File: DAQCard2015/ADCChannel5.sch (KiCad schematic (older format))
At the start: 50 parts, among them U10 LTC6403, U6 LTC6403, U7 AD9219, U8 LTC6403, U9 LTC6403

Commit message: Replaces single ample with 4-channel varients. Greatly reducing part count
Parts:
- removed C23, C33, C37, C38: .01uF, symbol C
- removed C24, C25, C29, C31, C32: .1uF, symbol C
- removed C26, C27, C28, C34, C35, C36, C39, C40, C41, C42, C43, C44: C, symbol C
- removed C30: 2.2uF, symbol CP
- removed R25, R32, R37, R38: Rt, symbol R
- removed R26, R27, R33, R34, R39, R40, R41, R42: Ri, symbol R
- removed R29, R30, R35, R36, R43, R44, R45: Rf, symbol R
- removed R31: 10k, symbol R
- removed U10, U6, U8, U9: LTC6403, symbol LTC6403
- removed U7: AD9219, symbol AD9219
- added C62, C63, C64: C, symbol C
- added C65: .01uF, symbol C
- added C66, C67, C68, C70, C71: .1uF, symbol C
- added C69: 2.2uF, symbol CP
- added R49: Rt, symbol R
- added R50: 2.7k, symbol R
- added R51: 1k, symbol R
- added R52: 10k, symbol R
- added RP19: R_PACK8, symbol R_PACK8
- added RP20, RP21: Rf, symbol R_PACK4
- added U14: THS4524IDBTR, symbol THS4524IDBTR
- added U15: AD9219, symbol AD9219
- R46: value Rf -> Rt
- R47: value 2.7k -> Rt
- R48: value 1k -> Rt
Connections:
- net labels added: 3V3ana, VOCM
- net labels removed: 18ana, 3V3, Vocm
- wire segments 178 -> 192
- no-connect marks 12 -> 4
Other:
- note removed: "100R Termination \nis common for all ADCs."

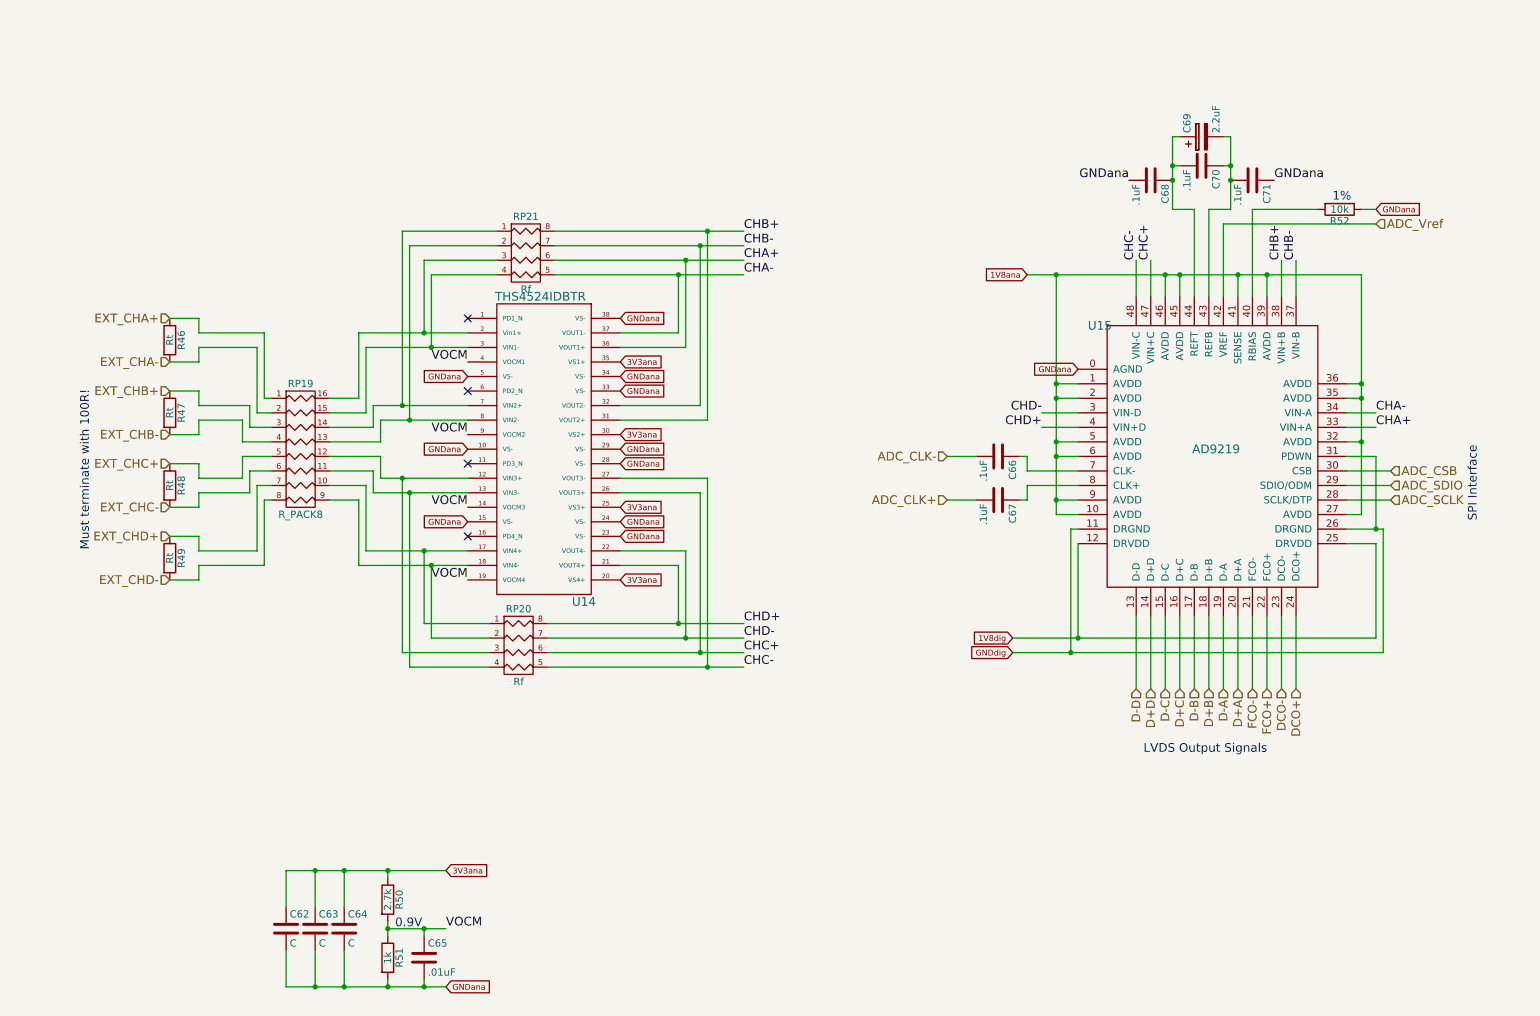
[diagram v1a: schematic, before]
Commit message: Finishes initial version of schematic(mostly). And adds a whole bunch of new footprints!
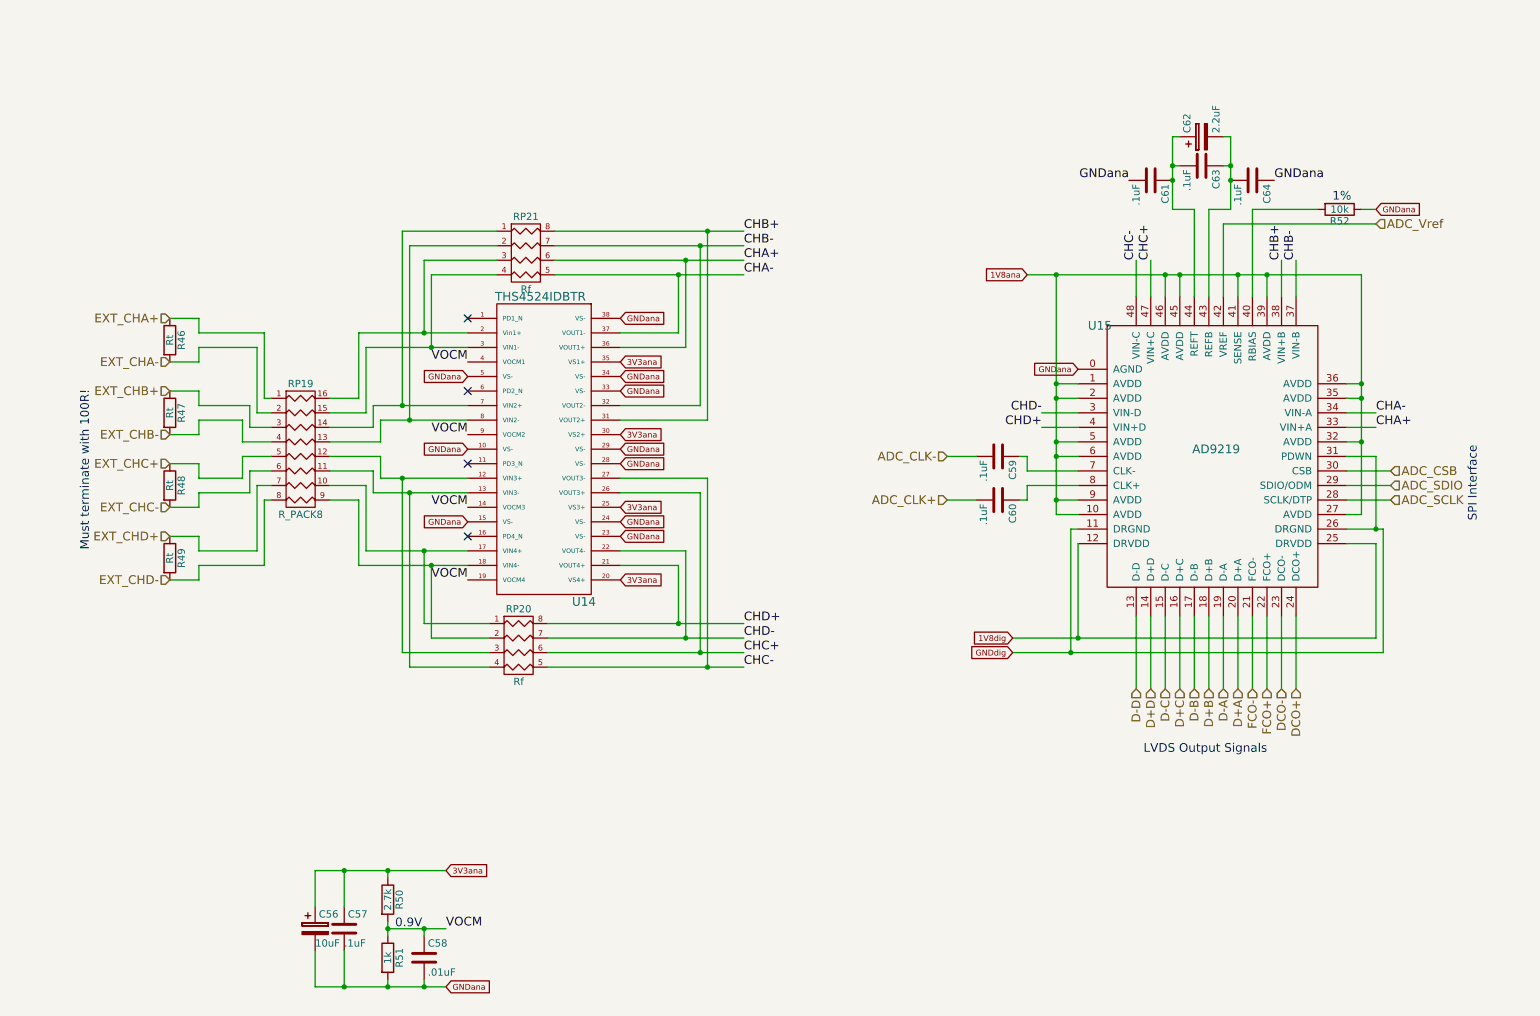
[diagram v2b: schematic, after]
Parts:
- removed C62: C, symbol C
- removed C65: .01uF, symbol C
- removed C66, C67, C68, C70, C71: .1uF, symbol C
- removed C69: 2.2uF, symbol CP
- added C56: 10uF, extras:SMD_Cap_3mmDia, symbol CP
- added C57, C59, C60, C61: .1uF, Capacitors_SMD:C_0603, symbol C
- added C58: .01uF, Capacitors_SMD:C_0603, symbol C
- added C62: 2.2uF, extras:SMD_Cap_3mmDia, symbol CP
- C63, C64: value C -> .1uF; footprint (none) -> Capacitors_SMD:C_0603
- R46, R47, R48, R49, R50, R51, R52: footprint (none) -> Resistors_SMD:R_0603
- RP19: footprint (none) -> extras:R8_MNR18
- RP20, RP21: footprint (none) -> extras:R4-MNR04
- U14: footprint (none) -> Housings_SSOP:TSSOP-38_4.4x9.7mm_Pitch0.5mm
- U15: footprint (none) -> SMD_Packages:QFN-48-1EP
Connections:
- net 3V3ana: now also C56.1, C57.1; no longer C63.1, C64.1
- net ADC_CLK+: now also C60.2
- net ADC_CLK-: now also C59.2
- net GNDana: now also C64.1, C56.2, C57.2, C58.2, C61.2; no longer C63.2, C64.2
- net VOCM: now also C58.1
- net at U15.43 (REFB): now also C63.1, C64.2, C62.2
- net at U15.44 (REFT): now also C63.2, C61.1, C62.1
- net at U15.7 (CLK-): now also C59.1
- net at U15.8 (CLK+): now also C60.1
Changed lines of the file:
@@
 $Comp
 L AD9219 U15
-U 1 1 55CFF5B1
+U 1 1 55CB5756
 P 9050 3700
 F 0 "U15" H 8250 4650 60  0000 C CNN
 F 1 "AD9219" H 9050 3800 60  0000 C CNN
-F 2 "" H 8650 3700 60  0000 C CNN
+F 2 "SMD_Packages:QFN-48-1EP" H 8650 3700 60  0001 C CNN
 F 3 "" H 8650 3700 60  0000 C CNN
 	1    9050 3700
@@
 $Comp
 L R R50
-U 1 1 55CFF5F2
+U 1 1 55CB5789
 P 3350 6700
 F 0 "R50" V 3430 6700 50  0000 C CNN
 F 1 "2.7k" V 3350 6700 50  0000 C CNN
-F 2 "" V 3280 6700 30  0000 C CNN
+F 2 "Resistors_SMD:R_0603" V 3280 6700 30  0001 C CNN
 F 3 "" H 3350 6700 30  0000 C CNN
 	1    3350 6700
@@
 $Comp
 L R R51
-U 1 1 55CFF5DF
+U 1 1 55CB5777
 P 3350 7100
 F 0 "R51" V 3430 7100 50  0000 C CNN
 F 1 "1k" V 3350 7100 50  0000 C CNN
-F 2 "" V 3280 7100 30  0000 C CNN
+F 2 "Resistors_SMD:R_0603" V 3280 7100 30  0001 C CNN
 F 3 "" H 3350 7100 30  0000 C CNN
 	1    3350 7100
@@
 Must terminate with 100R!
 $Comp
-L C C62
-U 1 1 55C98F9B
-P 2650 6900
-F 0 "C62" H 2675 7000 50  0000 L CNN
-F 1 "C" H 2675 6800 50  0000 L CNN
-F 2 "" H 2688 6750 30  0000 C CNN
-F 3 "" H 2650 6900 60  0000 C CNN
-	1    2650 6900
-	1    0    0    -1
-$EndComp
-$Comp
-L C C63
-U 1 1 55CFF5B2
-P 2850 6900
-F 0 "C63" H 2875 7000 50  0000 L CNN
-F 1 "C" H 2875 6800 50  0000 L CNN
-F 2 "" H 2888 6750 30  0000 C CNN
-F 3 "" H 2850 6900 60  0000 C CNN
-	1    2850 6900
-	1    0    0    -1
-$EndComp
-$Comp
-L C C64
-U 1 1 55CFF5B9
+L C C57
+U 1 1 55CB575E
 P 3050 6900
-F 0 "C64" H 3075 7000 50  0000 L CNN
-F 1 "C" H 3075 6800 50  0000 L CNN
-F 2 "" H 3088 6750 30  0000 C CNN
+F 0 "C57" H 3075 7000 50  0000 L CNN
+F 1 ".1uF" H 3050 6800 50  0000 L CNN
+F 2 "Capacitors_SMD:C_0603" H 3088 6750 30  0001 C CNN
 F 3 "" H 3050 6900 60  0000 C CNN
 	1    3050 6900
@@
 ADC_SCLK
 $Comp
-L C C66
-U 1 1 55CFF5C5
+L C C59
+U 1 1 55CB5761
 P 7550 3650
-F 0 "C66" H 7575 3750 50  0000 L CNN
+F 0 "C59" H 7575 3750 50  0000 L CNN
 F 1 ".1uF" H 7575 3550 50  0000 L CNN
-F 2 "" H 7588 3500 30  0000 C CNN
+F 2 "Capacitors_SMD:C_0603" H 7588 3500 30  0001 C CNN
 F 3 "" H 7550 3650 60  0000 C CNN
 	1    7550 3650
@@
 $EndComp
 $Comp
-L C C67
-U 1 1 55CFF5E9
+L C C60
+U 1 1 55CB5747
 P 7550 3950
-F 0 "C67" H 7575 4050 50  0000 L CNN
+F 0 "C60" H 7575 4050 50  0000 L CNN
 F 1 ".1uF" H 7575 3850 50  0000 L CNN
-F 2 "" H 7588 3800 30  0000 C CNN
+F 2 "Capacitors_SMD:C_0603" H 7588 3800 30  0001 C CNN
 F 3 "" H 7550 3950 60  0000 C CNN
 	1    7550 3950
@@
 DCO+
 $Comp
-L C C71
-U 1 1 55CE4162
+L C C64
+U 1 1 55CB578B
 P 9300 1750
-F 0 "C71" H 9325 1850 50  0000 L CNN
+F 0 "C64" H 9325 1850 50  0000 L CNN
 F 1 ".1uF" H 9325 1650 50  0000 L CNN
-F 2 "" H 9338 1600 30  0000 C CNN
+F 2 "Capacitors_SMD:C_0603" H 9338 1600 30  0001 C CNN
 F 3 "" H 9300 1750 60  0000 C CNN
 	1    9300 1750
@@
 $EndComp
 $Comp
-L C C68
-U 1 1 55CFF5D2
+L C C61
+U 1 1 55CB576D
 P 8600 1750
-F 0 "C68" H 8625 1850 50  0000 L CNN
+F 0 "C61" H 8625 1850 50  0000 L CNN
 F 1 ".1uF" H 8625 1650 50  0000 L CNN
-F 2 "" H 8638 1600 30  0000 C CNN
+F 2 "Capacitors_SMD:C_0603" H 8638 1600 30  0001 C CNN
 F 3 "" H 8600 1750 60  0000 C CNN
 	1    8600 1750
@@
 $EndComp
 $Comp
-L C C70
-U 1 1 55CFF5DA
+L C C63
+U 1 1 55CB5772
 P 8950 1650
-F 0 "C70" H 8975 1750 50  0000 L CNN
+F 0 "C63" H 8975 1750 50  0000 L CNN
 F 1 ".1uF" H 8975 1550 50  0000 L CNN
-F 2 "" H 8988 1500 30  0000 C CNN
+F 2 "Capacitors_SMD:C_0603" H 8988 1500 30  0001 C CNN
 F 3 "" H 8950 1650 60  0000 C CNN
 	1    8950 1650
@@
 GNDana
 $Comp
-L CP C69
-U 1 1 55CFF601
+L CP C62
+U 1 1 55CB5794
 P 8950 1450
-F 0 "C69" H 8975 1550 50  0000 L CNN
+F 0 "C62" H 8975 1550 50  0000 L CNN
 F 1 "2.2uF" H 8975 1350 50  0000 L CNN
-F 2 "" H 8988 1300 30  0000 C CNN
+F 2 "extras:SMD_Cap_3mmDia" H 8988 1300 30  0001 C CNN
 F 3 "" H 8950 1450 60  0000 C CNN
 	1    8950 1450
@@
 $Comp
 L R R52
-U 1 1 55CFF5EF
+U 1 1 55CB577F
 P 9900 1950
 F 0 "R52" V 9980 1950 50  0000 C CNN
 F 1 "10k" V 9900 1950 50  0000 C CNN
-F 2 "" V 9830 1950 30  0000 C CNN
+F 2 "Resistors_SMD:R_0603" V 9830 1950 30  0001 C CNN
 F 3 "" H 9900 1950 30  0000 C CNN
 	1    9900 1950
@@
 $Comp
 L THS4524IDBTR U14
-U 1 1 55CFF607
+U 1 1 55CB579C
 P 4400 3700
 F 0 "U14" H 4700 2750 60  0000 C CNN
 F 1 "THS4524IDBTR" H 4400 4850 60  0000 C CNN
-F 2 "" H 4600 3800 60  0000 C CNN
+F 2 "Housings_SSOP:TSSOP-38_4.4x9.7mm_Pitch0.5mm" H 4600 3800 60  0001 C CNN
 F 3 "" H 4600 3800 60  0000 C CNN
 	1    4400 3700
@@
 $EndComp
 $Comp
-L C C65
-U 1 1 55CE6254
+L C C58
+U 1 1 55CB57A5
 P 3600 7100
-F 0 "C65" H 3625 7200 50  0000 L CNN
+F 0 "C58" H 3625 7200 50  0000 L CNN
 F 1 ".01uF" H 3625 7000 50  0000 L CNN
-F 2 "" H 3638 6950 30  0000 C CNN
+F 2 "Capacitors_SMD:C_0603" H 3638 6950 30  0001 C CNN
 F 3 "" H 3600 7100 60  0000 C CNN
 	1    3600 7100
@@
 Connection ~ 3600 6900
 Wire Wire Line
-	2650 6500 3750 6500
-Wire Wire Line
 	3050 6500 3050 6750
 Connection ~ 3350 6500
@@
 Connection ~ 3050 6500
 Wire Wire Line
-	2650 6500 2650 6750
-Connection ~ 2850 6500
-Wire Wire Line
-	2650 7300 3750 7300
-Wire Wire Line
 	3050 7300 3050 7050
 Wire Wire Line
 	2850 7300 2850 7050
 Connection ~ 3050 7300
-Wire Wire Line
-	2650 7300 2650 7050
-Connection ~ 2850 7300
 Wire Wire Line
 	3600 7300 3600 7250
@@
 $Comp
 L R R49
-U 1 1 55CF3372
+U 1 1 55CB57AB
 P 1850 4350
 F 0 "R49" V 1930 4350 50  0000 C CNN
 F 1 "Rt" V 1850 4350 50  0000 C CNN
-F 2 "" V 1780 4350 30  0000 C CNN
+F 2 "Resistors_SMD:R_0603" V 1780 4350 30  0001 C CNN
 F 3 "" H 1850 4350 30  0000 C CNN
 	1    1850 4350
@@
 $Comp
 L R R48
-U 1 1 55CFF620
+U 1 1 55CFF61B
 P 1850 3850
 F 0 "R48" V 1930 3850 50  0000 C CNN
 F 1 "Rt" V 1850 3850 50  0000 C CNN
-F 2 "" V 1780 3850 30  0000 C CNN
+F 2 "Resistors_SMD:R_0603" V 1780 3850 30  0001 C CNN
 F 3 "" H 1850 3850 30  0000 C CNN
 	1    1850 3850
@@
 $Comp
 L R R47
-U 1 1 55CF3D3D
+U 1 1 55CFF628
 P 1850 3350
 F 0 "R47" V 1930 3350 50  0000 C CNN
 F 1 "Rt" V 1850 3350 50  0000 C CNN
-F 2 "" V 1780 3350 30  0000 C CNN
+F 2 "Resistors_SMD:R_0603" V 1780 3350 30  0001 C CNN
 F 3 "" H 1850 3350 30  0000 C CNN
 	1    1850 3350
@@
 $Comp
 L R R46
-U 1 1 55CFF62F
+U 1 1 55CB57BE
 P 1850 2850
 F 0 "R46" V 1930 2850 50  0000 C CNN
 F 1 "Rt" V 1850 2850 50  0000 C CNN
-F 2 "" V 1780 2850 30  0000 C CNN
+F 2 "Resistors_SMD:R_0603" V 1780 2850 30  0001 C CNN
 F 3 "" H 1850 2850 30  0000 C CNN
 	1    1850 2850
@@
 $Comp
 L R_PACK4 RP20
-U 1 1 55CFF634
+U 1 1 55CB57C8
 P 4250 5150
 F 0 "RP20" H 4250 5600 50  0000 C CNN
 F 1 "Rf" H 4250 5100 50  0000 C CNN
-F 2 "" H 4250 5150 60  0000 C CNN
+F 2 "extras:R4-MNR04" H 4250 5150 60  0001 C CNN
 F 3 "" H 4250 5150 60  0000 C CNN
 	1    4250 5150
@@
 $Comp
 L R_PACK4 RP21
-U 1 1 55CFF63B
+U 1 1 55CB5750
 P 4300 2450
 F 0 "RP21" H 4300 2900 50  0000 C CNN
 F 1 "Rf" H 4300 2400 50  0000 C CNN
-F 2 "" H 4300 2450 60  0000 C CNN
+F 2 "extras:R4-MNR04" H 4300 2450 60  0001 C CNN
 F 3 "" H 4300 2450 60  0000 C CNN
 	1    4300 2450
@@
 $Comp
 L R_PACK8 RP19
-U 1 1 55CFF63F
+U 1 1 55CB57D0
 P 2750 3600
 F 0 "RP19" H 2750 4050 50  0000 C CNN
 F 1 "R_PACK8" H 2750 3150 50  0000 C CNN
-F 2 "" H 2750 3600 60  0000 C CNN
+F 2 "extras:R8_MNR18" H 2750 3600 60  0001 C CNN
 F 3 "" H 2750 3600 60  0000 C CNN
 	1    2750 3600
@@
 Text GLabel 10150 1950 2    40   Input ~ 0
 GNDana
+Wire Wire Line
+	3750 6500 2850 6500
+Wire Wire Line
+	2850 7300 3750 7300
+$Comp
+L CP C56
+U 1 1 55CB5742
+P 2850 6900
+F 0 "C56" H 2875 7000 50  0000 L CNN
+F 1 "10uF" H 2850 6800 50  0000 L CNN
+F 2 "extras:SMD_Cap_3mmDia" H 2888 6750 30  0001 C CNN
+F 3 "" H 2850 6900 60  0000 C CNN
+	1    2850 6900
+	1    0    0    -1
+$EndComp
 $EndSCHEMATC

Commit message: Adds a more-or-less complete BOM to DAQ Card
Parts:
- C58: value .01uF -> 10000pF
- RP19: value R_PACK8 -> Ri
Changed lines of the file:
@@
 $Descr A4 11693 8268
 encoding utf-8
-Sheet 3 13
+Sheet 9 13
 Title ""
 Date ""
@@
 P 3600 7100
 F 0 "C58" H 3625 7200 50  0000 L CNN
-F 1 ".01uF" H 3625 7000 50  0000 L CNN
+F 1 "10000pF" H 3625 7000 50  0000 L CNN
 F 2 "Capacitors_SMD:C_0603" H 3638 6950 30  0001 C CNN
 F 3 "" H 3600 7100 60  0000 C CNN
@@
 P 2750 3600
 F 0 "RP19" H 2750 4050 50  0000 C CNN
-F 1 "R_PACK8" H 2750 3150 50  0000 C CNN
+F 1 "Ri" H 2750 3150 50  0000 C CNN
 F 2 "extras:R8_MNR18" H 2750 3600 60  0001 C CNN
 F 3 "" H 2750 3600 60  0000 C CNN

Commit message: Updates to DAQCard2015, especially to power systems
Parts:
- C56, C62: footprint extras:SMD_Cap_3mmDia -> Capacitors_SMD:C_0805
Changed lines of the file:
@@
 F 0 "C62" H 8975 1550 50  0000 L CNN
 F 1 "2.2uF" H 8975 1350 50  0000 L CNN
-F 2 "extras:SMD_Cap_3mmDia" H 8988 1300 30  0001 C CNN
+F 2 "Capacitors_SMD:C_0805" H 8988 1300 30  0001 C CNN
 F 3 "" H 8950 1450 60  0000 C CNN
 	1    8950 1450
@@
 F 0 "C56" H 2875 7000 50  0000 L CNN
 F 1 "10uF" H 2850 6800 50  0000 L CNN
-F 2 "extras:SMD_Cap_3mmDia" H 2888 6750 30  0001 C CNN
+F 2 "Capacitors_SMD:C_0805" H 2888 6750 30  0001 C CNN
 F 3 "" H 2850 6900 60  0000 C CNN
 	1    2850 6900

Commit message: propogate previous changes to other channels and schematic
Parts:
- removed C56: 10uF, Capacitors_SMD:C_0805, symbol CP
- removed C57, C59, C60, C61, C63, C64: .1uF, Capacitors_SMD:C_0603, symbol C
- removed C58: 10000pF, Capacitors_SMD:C_0603, symbol C
- removed C62: 2.2uF, Capacitors_SMD:C_0805, symbol CP
- removed R46, R47, R48, R49: Rt, Resistors_SMD:R_0603, symbol R
- removed R50: 2.7k, Resistors_SMD:R_0603, symbol R
- removed R51: 1k, Resistors_SMD:R_0603, symbol R
- removed R52: 10k, Resistors_SMD:R_0603, symbol R
- removed RP19: Ri, extras:R8_MNR18, symbol R_PACK8
- removed RP20, RP21: Rf, extras:R4-MNR04, symbol R_PACK4
- removed U14: THS4524IDBTR, Housings_SSOP:TSSOP-38_4.4x9.7mm_Pitch0.5mm, symbol THS4524IDBTR
- removed U15: AD9219, SMD_Packages:QFN-48-1EP, symbol AD9219
- added C35, C36, C37, C39, C40: .1uF, Capacitors_SMD:C_0603, symbol C
- added C38: 2.2uF, Capacitors_SMD:C_0805, symbol C
- added R31, R32, R33, R34: Rt, Resistors_SMD:R_0603, symbol R
- added R35: 10k, Resistors_SMD:R_0603, symbol R
- added RP16: Ri, extras:R8_MNR18, symbol R_PACK8
- added RP17, RP18: Rf, extras:R4-MNR04, symbol R_PACK4
- added U13: THS4524IDBTR, Housings_SSOP:TSSOP-38_4.4x9.7mm_Pitch0.5mm, symbol THS4524IDBTR
- added U14: AD9219, extras:QFN-48-1EP, symbol AD9219
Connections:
- net 1V8ana: now also U14.1 (AVDD), U14.10 (AVDD), U14.2 (AVDD), U14.27 (AVDD), U14.32 (AVDD), U14.35 (AVDD), U14.36 (AVDD), U14.39 (AVDD), U14.41 (SENSE), U14.45 (AVDD), U14.46 (AVDD), U14.5 (AVDD), U14.6 (AVDD), U14.9 (AVDD)
- net 1V8dig: now also U14.12 (DRVDD), U14.25 (DRVDD)
- net 3V3ana: now also U13.20 (VS4+), U13.25 (VS3+), U13.30 (VS2+), U13.35 (VS1+)
- net ADC_CLK+: now also C36.2
- net ADC_CLK-: now also C35.2
- net ADC_CSB: now also U14.30 (CSB)
- net ADC_SCLK: now also U14.28 (SCLK/DTP)
- net ADC_SDIO: now also U14.29 (SDIO/ODM)
- net ADC_Vref: now also U14.42 (VREF)
- net CHA+: now also RP18.6 (R3), U13.36 (VOUT1+), U14.33 (VIN+A)
- net CHA-: now also RP18.5 (R4), U13.37 (VOUT1-), U14.34 (VIN-A)
- net CHB+: now also RP18.8 (R1), U13.31 (VOUT2+), U14.38 (VIN+B)
- net CHB-: now also RP18.7 (R2), U13.32 (VOUT2-), U14.37 (VIN-B)
- net CHC+: now also RP17.6 (R3), U13.26 (VOUT3+), U14.47 (VIN+C)
- net CHC-: now also RP17.5 (R4), U13.27 (VOUT3-), U14.48 (VIN-C)
- net CHD+: now also RP17.8 (R1), U13.21 (VOUT4+), U14.4 (VIN+D)
- net CHD-: now also RP17.7 (R2), U13.22 (VOUT4-), U14.3 (VIN-D)
- net D+A: now also U14.20 (D+A)
- net D+B: now also U14.18 (D+B)
- net D+C: now also U14.16 (D+C)
- net D+D: now also U14.14 (D+D)
- net D-A: now also U14.19 (D-A)
- net D-B: now also U14.17 (D-B)
- net D-C: now also U14.15 (D-C)
- net D-D: now also U14.13 (D-D)
- net DCO+: now also U14.24 (DCO+)
- net DCO-: now also U14.23 (DCO-)
- net EXT_CHA+: now also R31.1, RP16.1 (P1)
- net EXT_CHA-: now also R31.2, RP16.2 (P2)
- net EXT_CHB+: now also R32.1, RP16.3 (P3)
- net EXT_CHB-: now also R32.2, RP16.4 (P4)
- net EXT_CHC+: now also R33.1, RP16.5 (P5)
- net EXT_CHC-: now also R33.2, RP16.6 (P6)
- net EXT_CHD+: now also R34.1, RP16.7 (P7)
- net EXT_CHD-: now also R34.2, RP16.8 (P8)
- net FCO+: now also U14.22 (FCO+)
- net FCO-: now also U14.21 (FCO-)
- new net: R35.2, U14.40 (RBIAS)
- new net: C38.2, C39.1, C40.2, U14.43 (REFB)
- new net: C37.1, C38.1, C39.2, U14.44 (REFT)
- new net: C35.1, U14.7 (CLK-)
- new net: C36.1, U14.8 (CLK+)
- new net: RP16.10 (R7), RP17.3 (P3), U13.17 (VIN4+)
- new net: RP16.11 (R6), RP17.2 (P2), U13.13 (VIN3-)
- new net: RP16.12 (R5), RP17.1 (P1), U13.12 (VIN3+)
- new net: RP16.13 (R4), RP18.4 (P4), U13.8 (VIN2-)
- new net: RP16.14 (R3), RP18.3 (P3), U13.7 (VIN2+)
- new net: RP16.15 (R2), RP18.2 (P2), U13.3 (VIN1-)
- new net: RP16.16 (R1), RP18.1 (P1), U13.2 (Vin1+)
- new net: RP16.9 (R8), RP17.4 (P4), U13.18 (VIN4-)
- new net GND: C37.2, C40.1, R35.1, U13.10 (VS-), U13.15 (VS-), U13.23 (VS-), U13.24 (VS-), U13.28 (VS-), U13.29 (VS-), U13.33 (VS-), U13.34 (VS-), U13.38 (VS-), U13.5 (VS-), U14.0 (AGND), U14.11 (DRGND), U14.26 (DRGND), U14.31 (PDWN)
- new net Vocm: U13.14 (VOCM3), U13.19 (VOCM4), U13.4 (VOCM1), U13.9 (VOCM2)
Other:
- note added: "PD floating -> Power On"
- note removed: "0.9V"

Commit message: Various updates to DAQ board focusing on power system
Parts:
- U13: footprint Housings_SSOP:TSSOP-38_4.4x9.7mm_Pitch0.5mm -> extras:TSSOP-38_4.4x9.7mm_Pitch0.5mm
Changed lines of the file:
@@
 F 0 "U13" H 4700 2750 60  0000 C CNN
 F 1 "THS4524IDBTR" H 4400 4850 60  0000 C CNN
-F 2 "Housings_SSOP:TSSOP-38_4.4x9.7mm_Pitch0.5mm" H 4600 3800 60  0001 C CNN
+F 2 "extras:TSSOP-38_4.4x9.7mm_Pitch0.5mm" H 4600 3800 60  0001 C CNN
 F 3 "" H 4600 3800 60  0000 C CNN
 	1    4400 3700
